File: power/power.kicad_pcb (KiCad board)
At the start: 4 copper layers, 73.7 x 39.4 mm, 65 parts, among them M1 HIP2101, M2 HIP2101, M3 HIP2101, M4 ACS722, M5 ACS722, P1 PLS_10, P3 C, P4 A, P5 B, P6 VDD, P7 GND, P8 PLS_3, P9 PLS_3, Q1 CSD18532, Q2 CSD18532, Q3 CSD18532, Q4 CSD18532, Q5 CSD18532, Q6 CSD18532

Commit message: Going to make a rev2.
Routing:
- net +12V: track 46.8 -> 22.2 mm
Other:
- board text added: "PMC rev2"
- board text removed: "PMC rev.1"
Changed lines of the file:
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@@
     (thickness 2)
     (drawings 7)
-    (tracks 589)
+    (tracks 585)
     (zones 0)
     (modules 65)
@@
   (title_block
     (title "Phobia Power Board")
-    (date 2016-01-30)
-    (rev 1)
+    (date 2016-02-02)
+    (rev 2)
     (company "Roman Belov")
   )
@@
   (gr_line (start 196.215 121.285) (end 122.555 121.285) (layer Edge.Cuts) (width 0.15))
   (gr_line (start 196.215 81.915) (end 196.215 121.285) (layer Edge.Cuts) (width 0.15))
-  (gr_text "PMC\nrev.1" (at 192.405 112.395) (layer B.Cu)
+  (gr_text "PMC\nrev2" (at 192.405 112.395) (layer B.Cu)
     (effects (font (size 1.5 1.5) (thickness 0.3)) (justify mirror))
   )
@@
   (segment (start 155.3845 92.2655) (end 155.575 92.075) (width 0.508) (layer F.Cu) (net 1))
   (segment (start 155.3845 92.2655) (end 155.3845 95.25) (width 0.508) (layer F.Cu) (net 1) (status 20))
-  (segment (start 156.845 93.345) (end 168.402 93.345) (width 0.508) (layer B.Cu) (net 2))
-  (segment (start 168.402 93.345) (end 168.91 93.853) (width 0.508) (layer B.Cu) (net 2))
   (segment (start 184.15 93.853) (end 186.817 93.853) (width 0.508) (layer B.Cu) (net 2))
   (via (at 187.325 93.345) (size 0.889) (drill 0.4) (layers F.Cu B.Cu) (net 2))
   (segment (start 186.817 93.853) (end 187.325 93.345) (width 0.508) (layer B.Cu) (net 2))
-  (segment (start 172.085 93.345) (end 183.642 93.345) (width 0.508) (layer B.Cu) (net 2))
-  (segment (start 183.642 93.345) (end 184.15 93.853) (width 0.508) (layer B.Cu) (net 2))
   (segment (start 168.91 93.853) (end 171.577 93.853) (width 0.508) (layer B.Cu) (net 2))
   (via (at 172.085 93.345) (size 0.889) (drill 0.4) (layers F.Cu B.Cu) (net 2))
@@
   (segment (start 153.8605 95.25) (end 153.8605 93.6625) (width 0.508) (layer F.Cu) (net 11) (status 30))
   (segment (start 153.8605 93.6625) (end 153.543 93.345) (width 0.508) (layer F.Cu) (net 11) (status 30))
+  (segment (start 161.925 94.615) (end 159.385 92.075) (width 0.508) (layer B.Cu) (net 12))
+  (segment (start 159.385 92.075) (end 156.845 92.075) (width 0.508) (layer B.Cu) (net 12))
   (segment (start 160.2105 95.25) (end 161.29 95.25) (width 0.508) (layer F.Cu) (net 12))
+  (segment (start 161.29 95.25) (end 161.925 94.615) (width 0.508) (layer F.Cu) (net 12))
+  (via (at 161.925 94.615) (size 0.9) (drill 0.4) (layers F.Cu B.Cu) (net 12))
+  (via (at 156.845 92.075) (size 0.889) (drill 0.4) (layers F.Cu B.Cu) (net 12))
+  (segment (start 156.845 92.075) (end 156.845 91.44) (width 0.508) (layer F.Cu) (net 12))
+  (segment (start 156.845 91.44) (end 157.48 90.805) (width 0.508) (layer F.Cu) (net 12))
   (segment (start 157.48 90.805) (end 158.877 90.805) (width 0.508) (layer F.Cu) (net 12))
-  (segment (start 156.845 91.44) (end 157.48 90.805) (width 0.508) (layer F.Cu) (net 12))
-  (segment (start 156.845 92.075) (end 156.845 91.44) (width 0.508) (layer F.Cu) (net 12))
-  (via (at 156.845 92.075) (size 0.889) (drill 0.4) (layers F.Cu B.Cu) (net 12))
-  (segment (start 159.385 92.075) (end 156.845 92.075) (width 0.508) (layer In2.Cu) (net 12))
-  (segment (start 161.925 94.615) (end 159.385 92.075) (width 0.508) (layer In2.Cu) (net 12))
-  (via (at 161.925 94.615) (size 0.9) (drill 0.4) (layers F.Cu B.Cu) (net 12))
-  (segment (start 161.29 95.25) (end 161.925 94.615) (width 0.508) (layer F.Cu) (net 12))
   (segment (start 169.1005 95.25) (end 169.1005 93.6625) (width 0.508) (layer F.Cu) (net 13))
   (segment (start 169.1005 93.6625) (end 168.783 93.345) (width 0.508) (layer F.Cu) (net 13))
+  (segment (start 177.165 94.615) (end 174.625 92.075) (width 0.508) (layer B.Cu) (net 14))
+  (segment (start 174.625 92.075) (end 172.085 92.075) (width 0.508) (layer B.Cu) (net 14))
   (segment (start 175.4505 95.25) (end 176.53 95.25) (width 0.508) (layer F.Cu) (net 14))
   (segment (start 172.72 90.805) (end 174.117 90.805) (width 0.508) (layer F.Cu) (net 14))
@@
   (segment (start 172.085 92.075) (end 172.085 91.44) (width 0.508) (layer F.Cu) (net 14))
   (via (at 172.085 92.075) (size 0.889) (drill 0.4) (layers F.Cu B.Cu) (net 14))
-  (segment (start 174.625 92.075) (end 172.085 92.075) (width 0.508) (layer In2.Cu) (net 14))
-  (segment (start 177.165 94.615) (end 174.625 92.075) (width 0.508) (layer In2.Cu) (net 14))
   (via (at 177.165 94.615) (size 0.9) (drill 0.4) (layers F.Cu B.Cu) (net 14))
   (segment (start 176.53 95.25) (end 177.165 94.615) (width 0.508) (layer F.Cu) (net 14))
   (segment (start 184.3405 95.25) (end 184.3405 93.6625) (width 0.508) (layer F.Cu) (net 15))
   (segment (start 184.3405 93.6625) (end 184.023 93.345) (width 0.508) (layer F.Cu) (net 15))
+  (segment (start 192.405 94.615) (end 189.865 92.075) (width 0.508) (layer B.Cu) (net 16))
+  (segment (start 189.865 92.075) (end 187.325 92.075) (width 0.508) (layer B.Cu) (net 16))
   (segment (start 190.6905 95.25) (end 191.77 95.25) (width 0.508) (layer F.Cu) (net 16))
   (segment (start 187.96 90.805) (end 189.357 90.805) (width 0.508) (layer F.Cu) (net 16))
@@
   (segment (start 187.325 92.075) (end 187.325 91.44) (width 0.508) (layer F.Cu) (net 16))
   (via (at 187.325 92.075) (size 0.889) (drill 0.4) (layers F.Cu B.Cu) (net 16))
-  (segment (start 189.865 92.075) (end 187.325 92.075) (width 0.508) (layer In2.Cu) (net 16))
-  (segment (start 192.405 94.615) (end 189.865 92.075) (width 0.508) (layer In2.Cu) (net 16))
   (via (at 192.405 94.615) (size 0.9) (drill 0.4) (layers F.Cu B.Cu) (net 16))
   (segment (start 191.77 95.25) (end 192.405 94.615) (width 0.508) (layer F.Cu) (net 16))
@@
     (connect_pads (clearance 0.381))
     (min_thickness 0.254)
-    (fill yes (arc_segments 16) (thermal_gap 0.508) (thermal_bridge_width 0.508))
+    (fill yes (arc_segments 16) (thermal_gap 0.508) (thermal_bridge_width 0.889))
     (polygon
       (pts
@@
     (connect_pads (clearance 0.381))
     (min_thickness 0.254)
-    (fill yes (arc_segments 16) (thermal_gap 0.508) (thermal_bridge_width 0.508))
+    (fill yes (arc_segments 16) (thermal_gap 0.508) (thermal_bridge_width 0.889))
     (polygon
       (pts
@@
     (connect_pads (clearance 0.381))
     (min_thickness 0.254)
-    (fill yes (arc_segments 16) (thermal_gap 0.508) (thermal_bridge_width 0.508))
+    (fill yes (arc_segments 16) (thermal_gap 0.508) (thermal_bridge_width 0.889))
     (polygon
       (pts
@@
     (connect_pads (clearance 0.381))
     (min_thickness 0.254)
-    (fill yes (arc_segments 16) (thermal_gap 0.508) (thermal_bridge_width 0.508))
+    (fill yes (arc_segments 16) (thermal_gap 0.508) (thermal_bridge_width 0.889))
     (polygon
       (pts
@@
     (connect_pads (clearance 0.381))
     (min_thickness 0.254)
-    (fill yes (arc_segments 16) (thermal_gap 0.508) (thermal_bridge_width 0.508))
+    (fill yes (arc_segments 16) (thermal_gap 0.508) (thermal_bridge_width 0.889))
     (polygon
       (pts
@@
     (connect_pads (clearance 0.381))
     (min_thickness 0.254)
-    (fill yes (arc_segments 16) (thermal_gap 0.508) (thermal_bridge_width 0.508))
+    (fill yes (arc_segments 16) (thermal_gap 0.508) (thermal_bridge_width 0.889))
     (polygon
       (pts
@@
     (connect_pads (clearance 0.381))
     (min_thickness 0.254)
-    (fill yes (arc_segments 16) (thermal_gap 0.508) (thermal_bridge_width 0.508))
+    (fill yes (arc_segments 16) (thermal_gap 0.508) (thermal_bridge_width 0.889))
     (polygon
       (pts
@@
     (connect_pads (clearance 0.381))
     (min_thickness 0.254)
-    (fill yes (arc_segments 16) (thermal_gap 0.508) (thermal_bridge_width 0.508))
+    (fill yes (arc_segments 16) (thermal_gap 0.508) (thermal_bridge_width 0.889))
     (polygon
       (pts
@@
     (connect_pads (clearance 0.381))
     (min_thickness 0.254)
-    (fill yes (arc_segments 16) (thermal_gap 0.508) (thermal_bridge_width 0.508))
+    (fill yes (arc_segments 16) (thermal_gap 0.508) (thermal_bridge_width 0.889))
     (polygon
       (pts
@@
     (connect_pads (clearance 0.381))
     (min_thickness 0.254)
-    (fill yes (arc_segments 16) (thermal_gap 0.508) (thermal_bridge_width 0.508))
+    (fill yes (arc_segments 16) (thermal_gap 0.508) (thermal_bridge_width 0.889))
     (polygon
       (pts
@@
     (connect_pads (clearance 0.381))
     (min_thickness 0.254)
-    (fill yes (arc_segments 16) (thermal_gap 0.508) (thermal_bridge_width 0.508))
+    (fill yes (arc_segments 16) (thermal_gap 0.508) (thermal_bridge_width 0.889))
     (polygon
       (pts
@@
       )
     )
+  )
+  (zone (net 1) (net_name PGND) (layer F.Cu) (hatch edge 0.508)
+    (connect_pads (clearance 0.381))
+    (min_thickness 0.254)
+    (fill yes (arc_segments 16) (thermal_gap 0.508) (thermal_bridge_width 0.889))
+    (polygon
+      (pts
+        (xy 151.13 82.55) (xy 195.58 82.55) (xy 195.58 94.488) (xy 151.13 94.488)
+      )
+    )

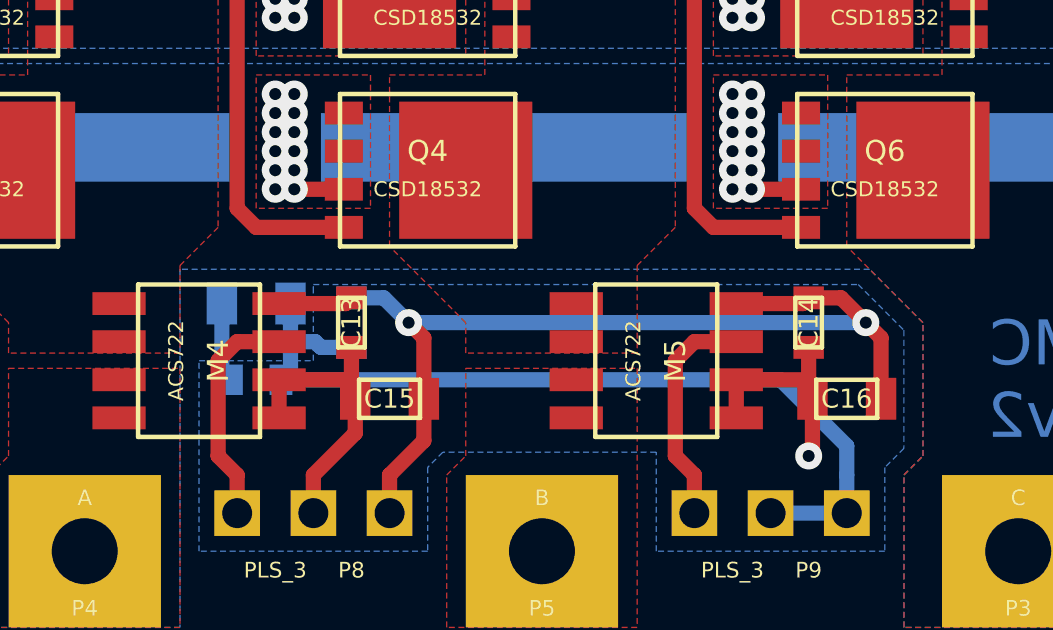
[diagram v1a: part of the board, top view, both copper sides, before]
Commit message: Small changes, enlarged supply rail clearance.
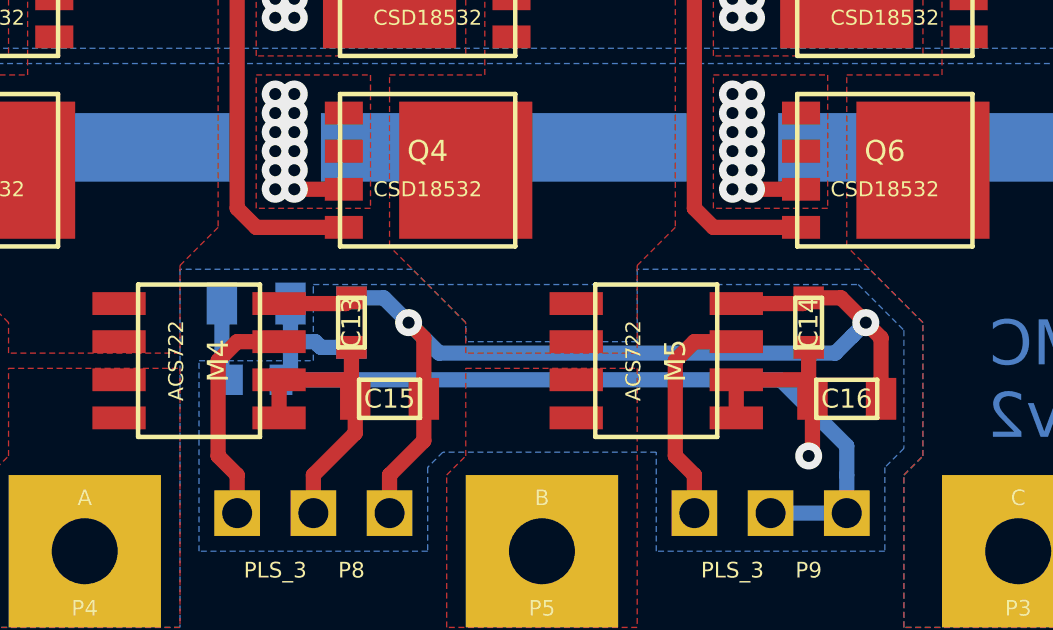
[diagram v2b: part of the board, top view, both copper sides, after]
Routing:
- net +3.3V: track 34.5 -> 35.3 mm
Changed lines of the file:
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@@
     (thickness 2)
     (drawings 7)
-    (tracks 585)
+    (tracks 588)
     (zones 0)
     (modules 65)
@@
   (segment (start 191.77 90.9955) (end 191.77 92.583) (width 0.508) (layer F.Cu) (net 8))
   (segment (start 191.77 92.583) (end 191.897 92.71) (width 0.508) (layer F.Cu) (net 8))
+  (segment (start 170.815 110.49) (end 171.83099 111.50599) (width 0.508) (layer B.Cu) (net 9))
+  (segment (start 171.83099 111.50599) (end 185.03901 111.50599) (width 0.508) (layer B.Cu) (net 9))
+  (segment (start 185.03901 111.50599) (end 185.605001 110.939999) (width 0.508) (layer B.Cu) (net 9))
+  (segment (start 185.605001 110.939999) (end 186.055 110.49) (width 0.508) (layer B.Cu) (net 9))
   (segment (start 170.815 110.49) (end 169.9895 109.6645) (width 0.508) (layer B.Cu) (net 9))
   (segment (start 169.9895 109.6645) (end 168.91 109.6645) (width 0.508) (layer B.Cu) (net 9))
-  (segment (start 170.815 110.49) (end 186.055 110.49) (width 0.508) (layer B.Cu) (net 9))
   (via (at 186.055 110.49) (size 0.9) (drill 0.4) (layers F.Cu B.Cu) (net 9))
   (via (at 170.815 110.49) (size 0.9) (drill 0.4) (layers F.Cu B.Cu) (net 9))
@@
       (pts
         (xy 195.58 120.65) (xy 187.325 120.65) (xy 187.325 115.57) (xy 187.96 114.935) (xy 187.96 110.49)
-        (xy 186.182 108.712) (xy 163.195 108.712) (xy 163.195 120.65) (xy 156.845 120.65) (xy 156.845 108.204)
+        (xy 186.182 108.712) (xy 178.435 108.712) (xy 178.435 111.125) (xy 172.72 111.125) (xy 172.72 110.49)
+        (xy 170.942 108.712) (xy 163.195 108.712) (xy 163.195 120.65) (xy 156.845 120.65) (xy 156.845 108.204)
         (xy 132.08 108.204) (xy 132.08 115.57) (xy 150.495 115.57) (xy 150.495 120.65) (xy 123.19 120.65)
         (xy 123.19 101.854) (xy 195.58 101.854) (xy 195.58 120.65)

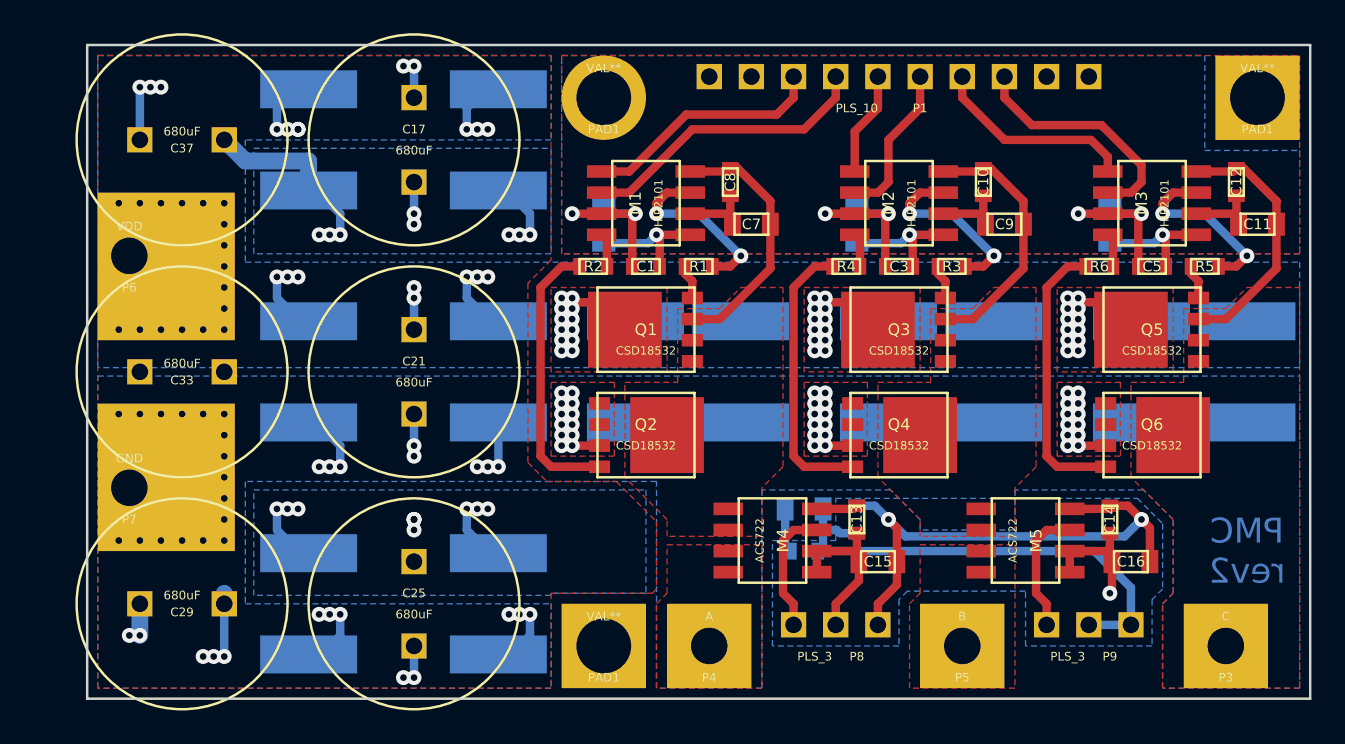
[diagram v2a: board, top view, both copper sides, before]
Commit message: Added OpAmp buffer, a lot of small fixes.
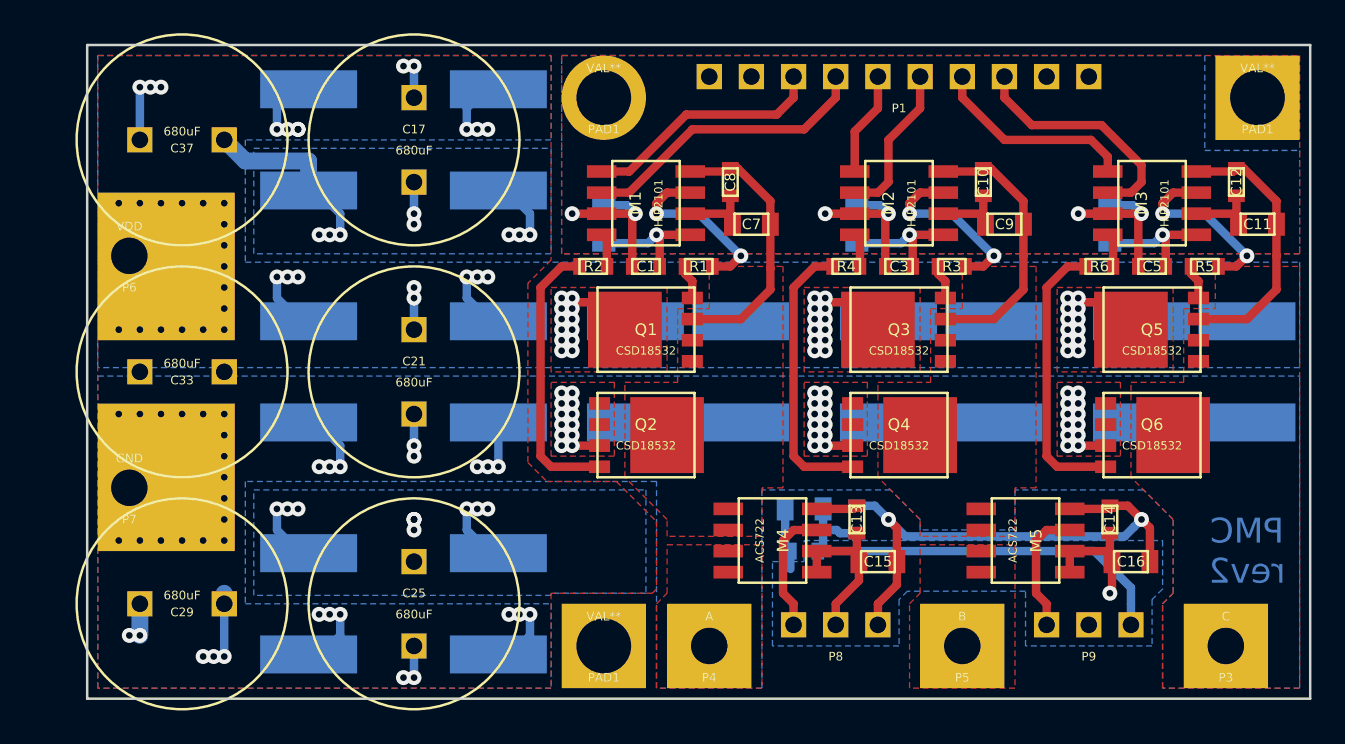
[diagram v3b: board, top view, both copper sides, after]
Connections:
- P9 pad 2: SENSOR_NTC -> Net-(P9-Pad2)
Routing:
- net SENSOR_NTC: track 29.3 -> 26.8 mm
- net AGND: track 19.7 -> 20.8 mm
- net Net-(C7-Pad1): track 15.7 -> 16.5 mm
- net Net-(C11-Pad1): track 15.7 -> 16.5 mm
- net Net-(C10-Pad1): track 15.7 -> 16.5 mm

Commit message: Accumulated changes, large track width, encoder/hall interface, etc.
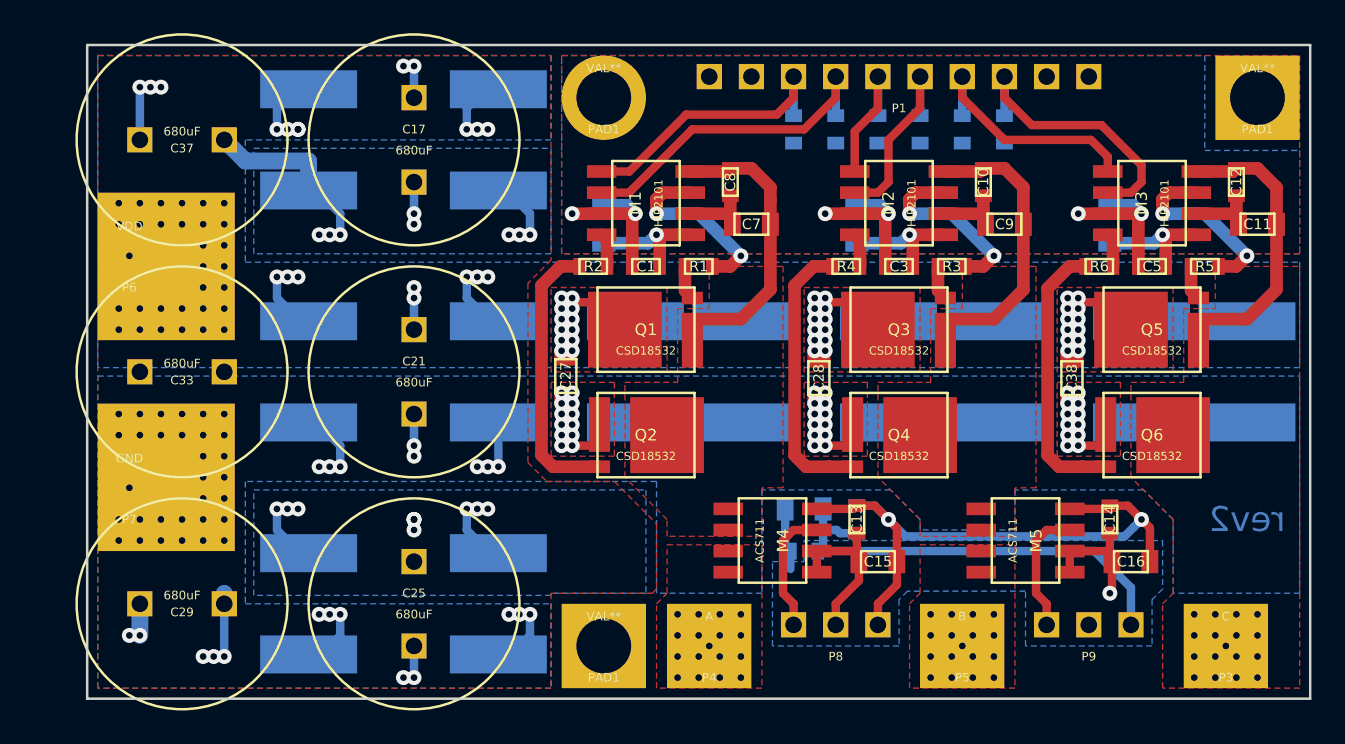
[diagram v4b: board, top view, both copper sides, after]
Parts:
- added C27: 0.1uF, foot:SM0805, F.Cu at (151.4, 101.9)
- added C28: 0.1uF, foot:SM0805, F.Cu at (166.6, 102.0)
- added C38: 0.1uF, foot:SM0805, F.Cu at (181.9, 102.0)
- added R10: 10K, foot:SM0603, B.Cu at (170.2, 87.0)
- added R11: 10K, foot:SM0603, B.Cu at (175.3, 87.0)
- added R12: 10K, foot:SM0603, B.Cu at (167.6, 87.0)
- added R13: 10K, foot:SM0603, B.Cu at (172.7, 87.0)
- added R14: 10K, foot:SM0603, B.Cu at (177.8, 87.0)
- added R9: 10K, foot:SM0603, B.Cu at (165.1, 87.0)
- M4, M5: value ACS722 -> ACS711
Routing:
- net Net-(C11-Pad1): track 16.5 -> 36.0 mm, vias 0 -> 16
- net Net-(M5-Pad3): track 0.00 -> 19.1 mm, vias 0 -> 16
- net Net-(M4-Pad3): track 0.00 -> 19.1 mm, vias 0 -> 16
- net +36V: track 121.4 -> 137.9 mm, vias 84 -> 97
- net PGND: track 127.6 -> 139.2 mm, vias 86 -> 99
- net +12V: track 22.2 -> 27.3 mm
- net FET_CL: track 14.5 -> 16.9 mm
- net FET_CH: track 12.5 -> 14.9 mm
- net FET_BL: track 9.43 -> 11.8 mm
- net FET_BH: track 6.80 -> 9.15 mm
- net FET_AL: track 17.7 -> 20.1 mm
- net FET_AH: track 14.7 -> 17.0 mm
- net +3.3V: track 35.3 -> 37.6 mm
- net Net-(C11-Pad2): track 4.83 -> 4.18 mm
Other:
- board text added: "rev2"
- board text removed: "PMC rev2"
